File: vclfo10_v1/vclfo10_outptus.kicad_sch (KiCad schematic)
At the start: 33 parts, among them Q2 BC547, U6 TL072, U7 TL072

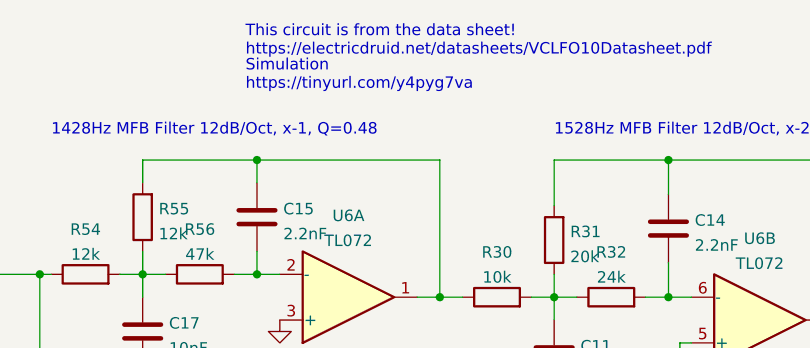
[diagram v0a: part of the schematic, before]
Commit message: Moved pcb files to sub folder
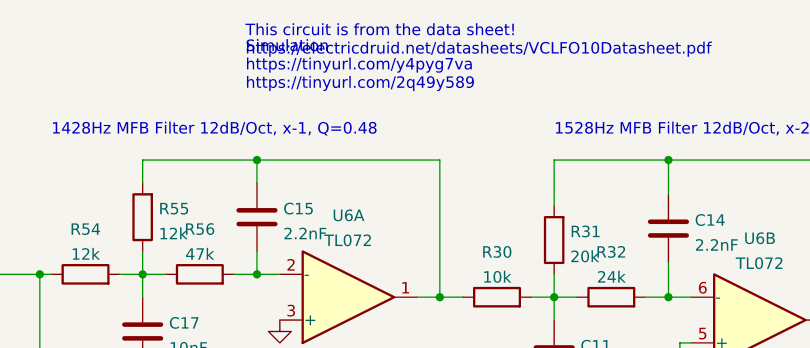
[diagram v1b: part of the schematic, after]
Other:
- note added: "Simulation https://tinyurl.com/y4pyg7va https://tinyurl.com/2q49y589"
- note removed: "Simulation https://tinyurl.com/y4pyg7va"
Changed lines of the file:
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@@
     (effects (font (size 1.27 1.27)) (justify left bottom))
   )
-  (text "Simulation \nhttps://tinyurl.com/y4pyg7va" (at 127 38.1 0)
+  (text "Simulation \nhttps://tinyurl.com/y4pyg7va\nhttps://tinyurl.com/2q49y589"
+    (at 127 38.1 0)
     (effects (font (size 1.27 1.27)) (justify left bottom))
   )
